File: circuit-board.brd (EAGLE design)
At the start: 100 x 80 mm, 39 parts, among them Q1 BC547B, U1 MAX3232, U2 ATMEGA328P_TQFP, U3 ADUM1201BRZ, Y1 16MHz

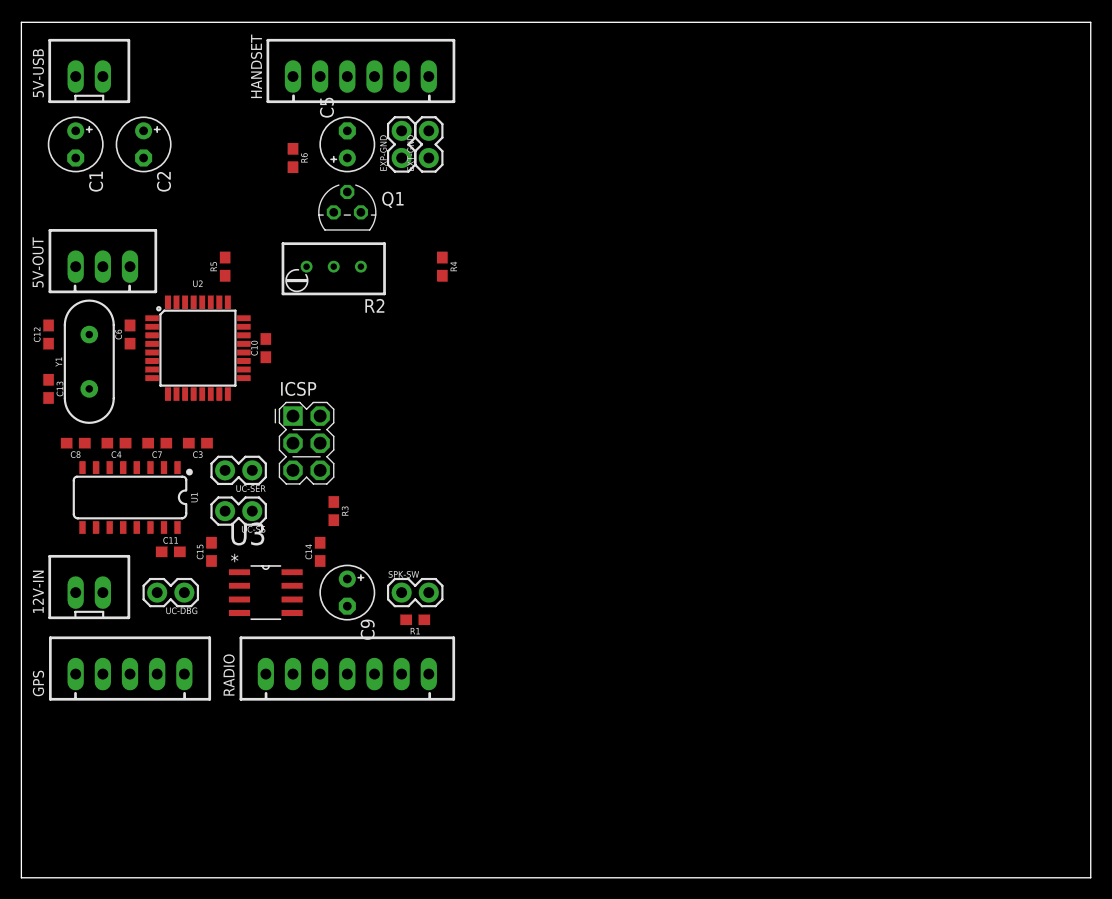
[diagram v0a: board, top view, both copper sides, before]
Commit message: Done for tonight, PCB laid out, need to verify ERC/DRC tomorrow
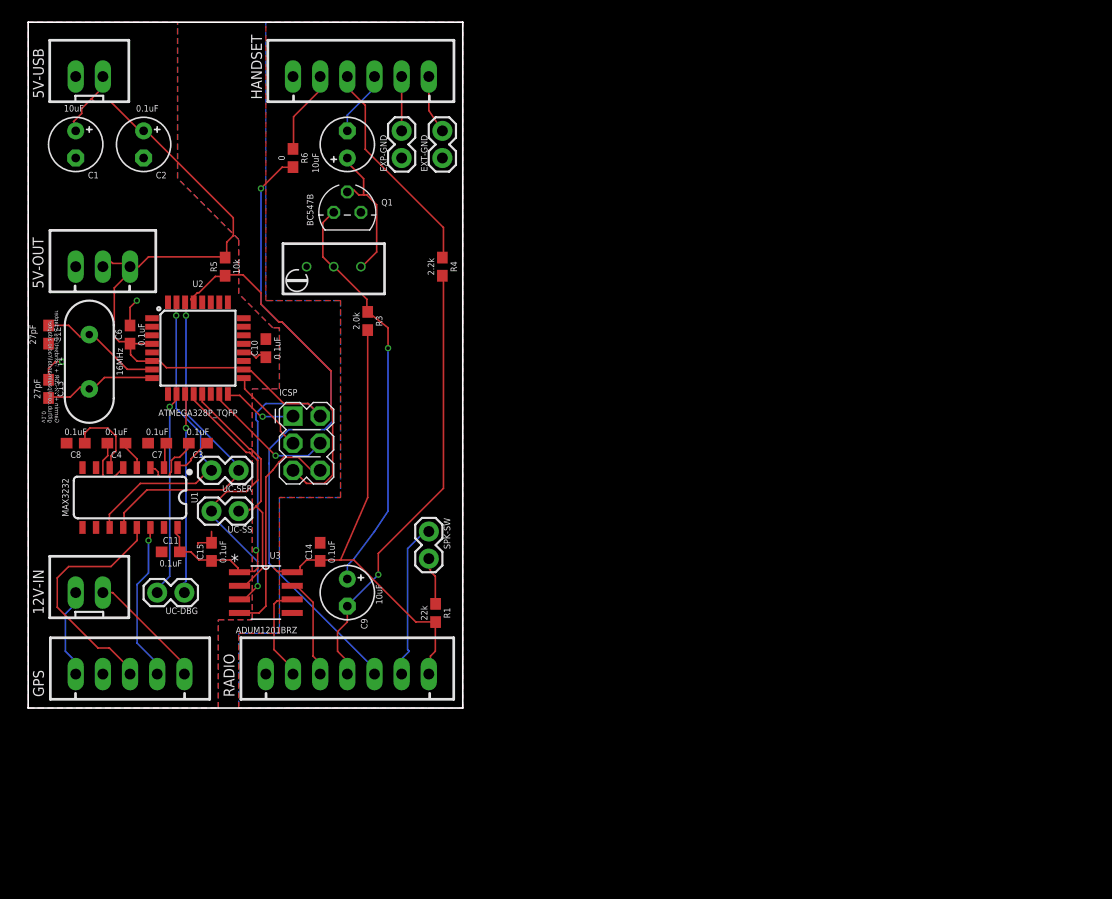
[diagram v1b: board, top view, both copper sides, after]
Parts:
- moved R3 18.1 mm to (32.4, 52.1)
- moved SPK-SW 6.25 mm to (38.1, 32.4), turned to 270 degrees
- moved R1 2.01 mm to (38.7, 24.8), turned to 270 degrees
- moved UC-SER 1.27 mm to (20.3, 38.1)
- moved UC-SS 1.27 mm to (20.3, 34.3)
- moved EXT-GND 1.27 mm to (39.4, 67.3)
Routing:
- net +5V: track 0.00 -> 105.3 mm, vias 0 -> 1
- net RADIO-SPK-OUT: track 0.00 -> 60.8 mm, vias 0 -> 1
- net 3.3V: track 0.00 -> 45.6 mm
- net RADIO-MIC/PTT: track 0.00 -> 41.8 mm, vias 0 -> 1
- net N$3: track 0.00 -> 38.8 mm, vias 0 -> 1
- net UC-RESET: track 0.00 -> 33.6 mm
- net UC-RX: track 0.00 -> 31.9 mm, vias 0 -> 1
- net UC-TX: track 0.00 -> 29.7 mm, vias 0 -> 1
- net GNDA: track 0.00 -> 28.9 mm, vias 0 -> 2
- net UC-SS-TX: track 0.00 -> 27.5 mm, vias 0 -> 1
- net UC-SS-RX: track 0.00 -> 23.8 mm
- net GPS-TX: track 0.00 -> 22.6 mm
- net HANDSET-PTT: track 0.00 -> 20.7 mm
- net UC-DBG-TX: track 0.00 -> 19.4 mm, vias 0 -> 1
- net UC-DBG-RX: track 0.00 -> 18.7 mm, vias 0 -> 1
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- added copper zone on layer 1, net GND
- added copper zone on layer 16, net GND
- added copper zone on layer 1, net GNDA
- added copper zone on layer 16, net GNDA
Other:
- board size 100 x 80 mm -> 40.6 x 64.1 mm
- board text added: "Garmin + VX-8DR + Handset/Mic Adapter github.com/paulmandal/radio-adapter v1.0"
